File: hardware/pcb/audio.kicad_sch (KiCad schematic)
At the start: 18 parts, among them IC3 TAC5212, J4 PJ-342, J5 PJ-242

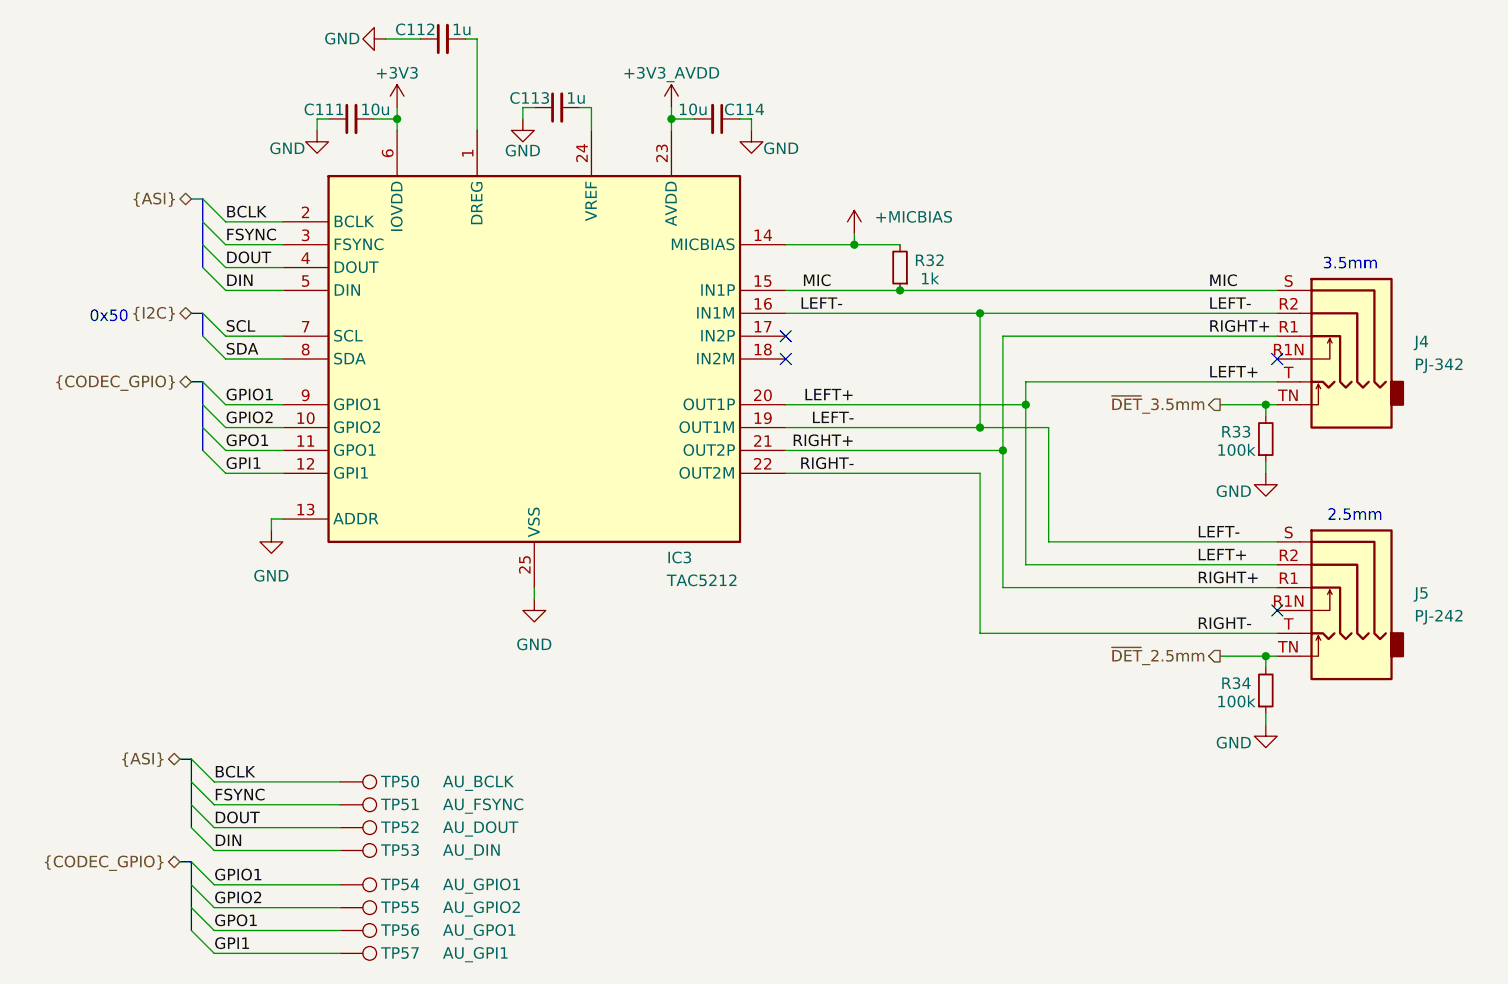
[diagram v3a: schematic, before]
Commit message: added capacitor to sama ddr vref pin
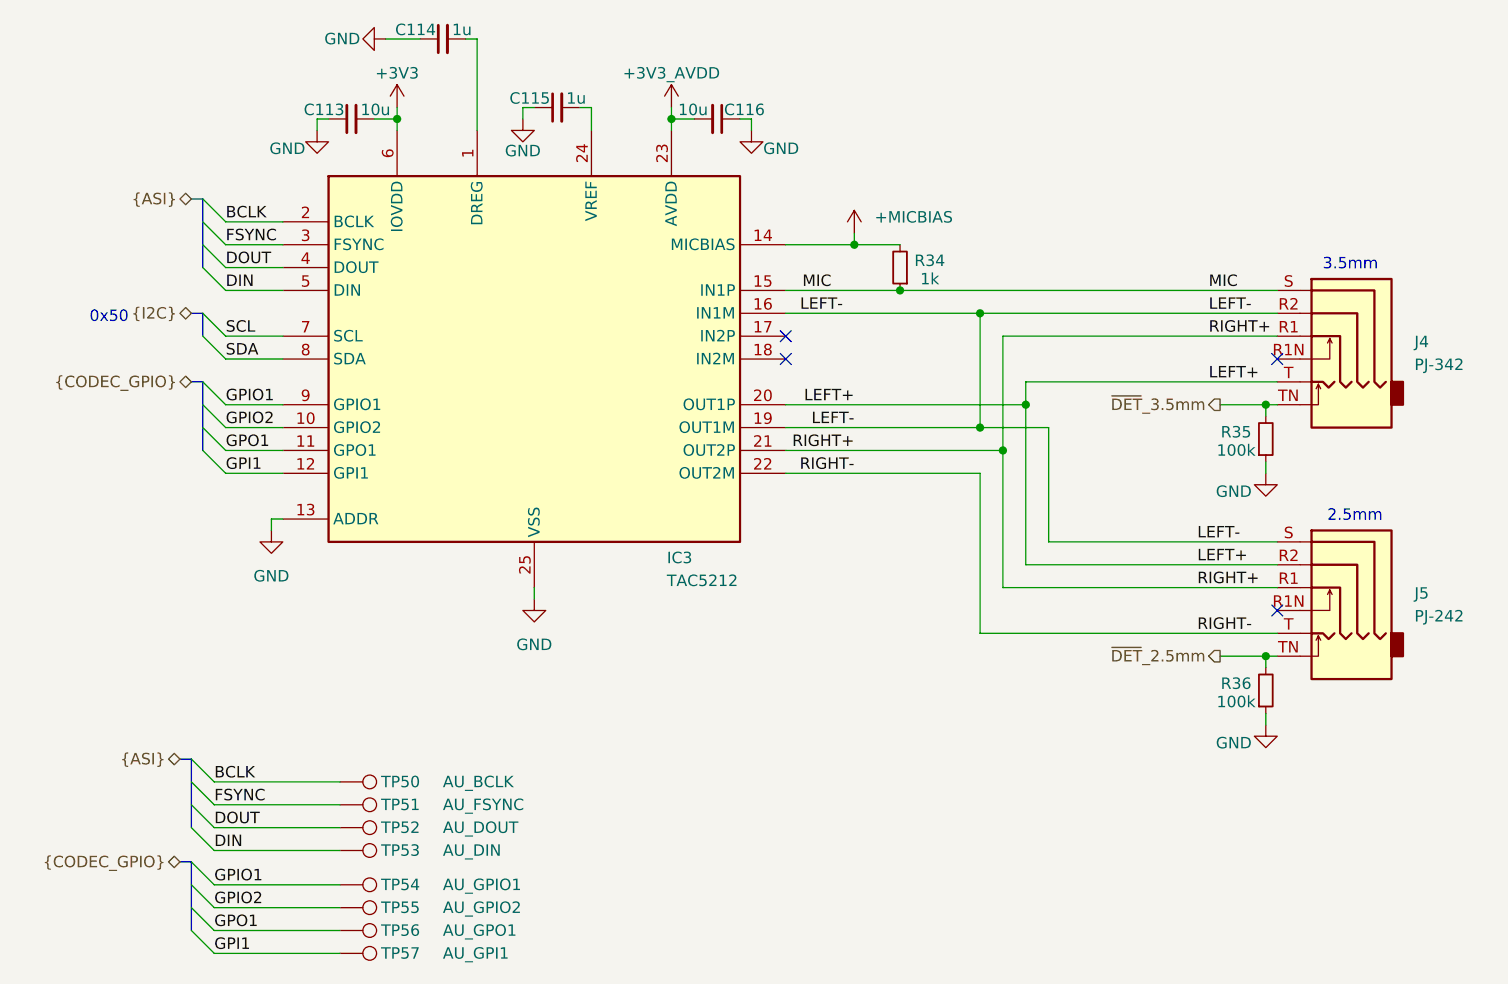
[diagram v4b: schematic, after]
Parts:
- renumbered C111 to C113, C112 to C114, C113 to C115, C114 to C116, R32 to R34, R33 to R35, R34 to R36
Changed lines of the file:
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@@
 		(in_pos_files yes)
 		(dnp no)
-		(property "Reference" "#PWR0106"
+		(property "Reference" "#PWR0108"
 			(at 58.42 33.02 0)
 			(hide yes)
@@
 			(project "meko"
 				(path "/da54f10a-146b-4941-a9c7-55c7173bb101/073f6085-34ed-486a-9dc9-0ac1ede2fab6"
-					(reference "#PWR0106")
+					(reference "#PWR0108")
 					(unit 1)
 				)
@@
 		(in_pos_files yes)
 		(dnp no)
-		(property "Reference" "C111"
+		(property "Reference" "C113"
 			(at 52.578 29.464 90)
 			(show_name no)
@@
 			(project "meko"
 				(path "/da54f10a-146b-4941-a9c7-55c7173bb101/073f6085-34ed-486a-9dc9-0ac1ede2fab6"
-					(reference "C111")
+					(reference "C113")
 					(unit 1)
 				)
@@
 		(in_pos_files yes)
 		(dnp no)
-		(property "Reference" "C112"
+		(property "Reference" "C114"
 			(at 62.738 20.574 90)
 			(show_name no)
@@
 			(project "meko"
 				(path "/da54f10a-146b-4941-a9c7-55c7173bb101/073f6085-34ed-486a-9dc9-0ac1ede2fab6"
-					(reference "C112")
+					(reference "C114")
 					(unit 1)
 				)
@@
 		(dnp no)
 		(fields_autoplaced yes)
-		(property "Reference" "#PWR0103"
+		(property "Reference" "#PWR0105"
 			(at 44.45 82.55 0)
 			(hide yes)
@@
 			(project "meko"
 				(path "/da54f10a-146b-4941-a9c7-55c7173bb101/073f6085-34ed-486a-9dc9-0ac1ede2fab6"
-					(reference "#PWR0103")
+					(reference "#PWR0105")
 					(unit 1)
 				)
@@
 		(in_pos_files yes)
 		(dnp no)
-		(property "Reference" "#PWR0110"
+		(property "Reference" "#PWR0112"
 			(at 97.79 38.1 0)
 			(hide yes)
@@
 			(project "meko"
 				(path "/da54f10a-146b-4941-a9c7-55c7173bb101/073f6085-34ed-486a-9dc9-0ac1ede2fab6"
-					(reference "#PWR0110")
+					(reference "#PWR0112")
 					(unit 1)
 				)
@@
 		(in_pos_files yes)
 		(dnp no)
-		(property "Reference" "R34"
+		(property "Reference" "R36"
 			(at 151.638 93.218 0)
 			(show_name no)
@@
 			(project "meko"
 				(path "/da54f10a-146b-4941-a9c7-55c7173bb101/073f6085-34ed-486a-9dc9-0ac1ede2fab6"
-					(reference "R34")
+					(reference "R36")
 					(unit 1)
 				)
@@
 		(in_pos_files yes)
 		(dnp no)
-		(property "Reference" "#PWR0109"
+		(property "Reference" "#PWR0111"
 			(at 88.9 33.02 0)
 			(hide yes)
@@
 			(project "meko"
 				(path "/da54f10a-146b-4941-a9c7-55c7173bb101/073f6085-34ed-486a-9dc9-0ac1ede2fab6"
-					(reference "#PWR0109")
+					(reference "#PWR0111")
 					(unit 1)
 				)
@@
 		(in_pos_files yes)
 		(dnp no)
-		(property "Reference" "R33"
+		(property "Reference" "R35"
 			(at 151.638 65.278 0)
 			(show_name no)
@@
 			(project "meko"
 				(path "/da54f10a-146b-4941-a9c7-55c7173bb101/073f6085-34ed-486a-9dc9-0ac1ede2fab6"
-					(reference "R33")
+					(reference "R35")
 					(unit 1)
 				)
@@
 		(in_pos_files yes)
 		(dnp no)
-		(property "Reference" "#PWR0104"
+		(property "Reference" "#PWR0106"
 			(at 49.53 38.1 0)
 			(hide yes)
@@
 			(project "meko"
 				(path "/da54f10a-146b-4941-a9c7-55c7173bb101/073f6085-34ed-486a-9dc9-0ac1ede2fab6"
-					(reference "#PWR0104")
+					(reference "#PWR0106")
 					(unit 1)
 				)
@@
 		(in_pos_files yes)
 		(dnp no)
-		(property "Reference" "#PWR0112"
+		(property "Reference" "#PWR0114"
 			(at 154.94 76.2 0)
 			(hide yes)
@@
 			(project "meko"
 				(path "/da54f10a-146b-4941-a9c7-55c7173bb101/073f6085-34ed-486a-9dc9-0ac1ede2fab6"
-					(reference "#PWR0112")
+					(reference "#PWR0114")
 					(unit 1)
 				)
@@
 		(in_pos_files yes)
 		(dnp no)
-		(property "Reference" "#PWR0105"
+		(property "Reference" "#PWR0107"
 			(at 50.8 21.59 0)
 			(hide yes)
@@
 			(project "meko"
 				(path "/da54f10a-146b-4941-a9c7-55c7173bb101/073f6085-34ed-486a-9dc9-0ac1ede2fab6"
-					(reference "#PWR0105")
+					(reference "#PWR0107")
 					(unit 1)
 				)
@@
 		(in_pos_files yes)
 		(dnp no)
-		(property "Reference" "#PWR0107"
+		(property "Reference" "#PWR0109"
 			(at 72.39 36.83 0)
 			(hide yes)
@@
 			(project "meko"
 				(path "/da54f10a-146b-4941-a9c7-55c7173bb101/073f6085-34ed-486a-9dc9-0ac1ede2fab6"
-					(reference "#PWR0107")
+					(reference "#PWR0109")
 					(unit 1)
 				)
@@
 		(in_pos_files yes)
 		(dnp no)
-		(property "Reference" "C113"
+		(property "Reference" "C115"
 			(at 75.438 28.194 90)
 			(show_name no)
@@
 			(project "meko"
 				(path "/da54f10a-146b-4941-a9c7-55c7173bb101/073f6085-34ed-486a-9dc9-0ac1ede2fab6"
-					(reference "C113")
+					(reference "C115")
 					(unit 1)
 				)
@@
 		(in_pos_files yes)
 		(dnp no)
-		(property "Reference" "#PWR0111"
+		(property "Reference" "#PWR0113"
 			(at 109.22 46.99 0)
 			(hide yes)
@@
 			(project "meko"
 				(path "/da54f10a-146b-4941-a9c7-55c7173bb101/073f6085-34ed-486a-9dc9-0ac1ede2fab6"
-					(reference "#PWR0111")
+					(reference "#PWR0113")
 					(unit 1)
 				)
@@
 		(in_pos_files yes)
 		(dnp no)
-		(property "Reference" "C114"
+		(property "Reference" "C116"
 			(at 94.742 29.464 90)
 			(show_name no)
@@
 			(project "meko"
 				(path "/da54f10a-146b-4941-a9c7-55c7173bb101/073f6085-34ed-486a-9dc9-0ac1ede2fab6"
-					(reference "C114")
+					(reference "C116")
 					(unit 1)
 				)
@@
 		(dnp no)
 		(fields_autoplaced yes)
-		(property "Reference" "#PWR0108"
+		(property "Reference" "#PWR0110"
 			(at 73.66 90.17 0)
 			(hide yes)
@@
 			(project "meko"
 				(path "/da54f10a-146b-4941-a9c7-55c7173bb101/073f6085-34ed-486a-9dc9-0ac1ede2fab6"
-					(reference "#PWR0108")
+					(reference "#PWR0110")
 					(unit 1)
 				)
@@
 		(in_pos_files yes)
 		(dnp no)
-		(property "Reference" "R32"
+		(property "Reference" "R34"
 			(at 117.602 46.228 0)
 			(show_name no)
@@
 			(project "meko"
 				(path "/da54f10a-146b-4941-a9c7-55c7173bb101/073f6085-34ed-486a-9dc9-0ac1ede2fab6"
-					(reference "R32")
+					(reference "R34")
 					(unit 1)
 				)
@@
 		(in_pos_files yes)
 		(dnp no)
-		(property "Reference" "#PWR0113"
+		(property "Reference" "#PWR0115"
 			(at 154.94 104.14 0)
 			(hide yes)
@@
 			(project "meko"
 				(path "/da54f10a-146b-4941-a9c7-55c7173bb101/073f6085-34ed-486a-9dc9-0ac1ede2fab6"
-					(reference "#PWR0113")
-					(unit 1)
-				)
+					(reference "#PWR0115")
+					(unit 1)
+				)

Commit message: didn't save last time :sob:
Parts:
- renumbered C113 to C114, C114 to C115, C115 to C116, C116 to C117
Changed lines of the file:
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@@
 		(in_pos_files yes)
 		(dnp no)
-		(property "Reference" "#PWR0108"
+		(property "Reference" "#PWR0109"
 			(at 58.42 33.02 0)
 			(hide yes)
@@
 			(project "meko"
 				(path "/da54f10a-146b-4941-a9c7-55c7173bb101/073f6085-34ed-486a-9dc9-0ac1ede2fab6"
-					(reference "#PWR0108")
+					(reference "#PWR0109")
 					(unit 1)
 				)
@@
 		(in_pos_files yes)
 		(dnp no)
-		(property "Reference" "C113"
+		(property "Reference" "C114"
 			(at 52.578 29.464 90)
 			(show_name no)
@@
 			(project "meko"
 				(path "/da54f10a-146b-4941-a9c7-55c7173bb101/073f6085-34ed-486a-9dc9-0ac1ede2fab6"
-					(reference "C113")
+					(reference "C114")
 					(unit 1)
 				)
@@
 		(in_pos_files yes)
 		(dnp no)
-		(property "Reference" "C114"
+		(property "Reference" "C115"
 			(at 62.738 20.574 90)
 			(show_name no)
@@
 			(project "meko"
 				(path "/da54f10a-146b-4941-a9c7-55c7173bb101/073f6085-34ed-486a-9dc9-0ac1ede2fab6"
-					(reference "C114")
+					(reference "C115")
 					(unit 1)
 				)
@@
 		(dnp no)
 		(fields_autoplaced yes)
-		(property "Reference" "#PWR0105"
+		(property "Reference" "#PWR0106"
 			(at 44.45 82.55 0)
 			(hide yes)
@@
 			(project "meko"
 				(path "/da54f10a-146b-4941-a9c7-55c7173bb101/073f6085-34ed-486a-9dc9-0ac1ede2fab6"
-					(reference "#PWR0105")
+					(reference "#PWR0106")
 					(unit 1)
 				)
@@
 		(in_pos_files yes)
 		(dnp no)
-		(property "Reference" "#PWR0112"
+		(property "Reference" "#PWR0113"
 			(at 97.79 38.1 0)
 			(hide yes)
@@
 			(project "meko"
 				(path "/da54f10a-146b-4941-a9c7-55c7173bb101/073f6085-34ed-486a-9dc9-0ac1ede2fab6"
-					(reference "#PWR0112")
+					(reference "#PWR0113")
 					(unit 1)
 				)
@@
 		(in_pos_files yes)
 		(dnp no)
-		(property "Reference" "#PWR0111"
+		(property "Reference" "#PWR0112"
 			(at 88.9 33.02 0)
 			(hide yes)
@@
 			(project "meko"
 				(path "/da54f10a-146b-4941-a9c7-55c7173bb101/073f6085-34ed-486a-9dc9-0ac1ede2fab6"
-					(reference "#PWR0111")
+					(reference "#PWR0112")
 					(unit 1)
 				)
@@
 		(in_pos_files yes)
 		(dnp no)
-		(property "Reference" "#PWR0106"
+		(property "Reference" "#PWR0107"
 			(at 49.53 38.1 0)
 			(hide yes)
@@
 			(project "meko"
 				(path "/da54f10a-146b-4941-a9c7-55c7173bb101/073f6085-34ed-486a-9dc9-0ac1ede2fab6"
-					(reference "#PWR0106")
+					(reference "#PWR0107")
 					(unit 1)
 				)
@@
 		(in_pos_files yes)
 		(dnp no)
-		(property "Reference" "#PWR0114"
+		(property "Reference" "#PWR0115"
 			(at 154.94 76.2 0)
 			(hide yes)
@@
 			(project "meko"
 				(path "/da54f10a-146b-4941-a9c7-55c7173bb101/073f6085-34ed-486a-9dc9-0ac1ede2fab6"
-					(reference "#PWR0114")
+					(reference "#PWR0115")
 					(unit 1)
 				)
@@
 		(in_pos_files yes)
 		(dnp no)
-		(property "Reference" "#PWR0107"
+		(property "Reference" "#PWR0108"
 			(at 50.8 21.59 0)
 			(hide yes)
@@
 			(project "meko"
 				(path "/da54f10a-146b-4941-a9c7-55c7173bb101/073f6085-34ed-486a-9dc9-0ac1ede2fab6"
-					(reference "#PWR0107")
+					(reference "#PWR0108")
 					(unit 1)
 				)
@@
 		(in_pos_files yes)
 		(dnp no)
-		(property "Reference" "#PWR0109"
+		(property "Reference" "#PWR0110"
 			(at 72.39 36.83 0)
 			(hide yes)
@@
 			(project "meko"
 				(path "/da54f10a-146b-4941-a9c7-55c7173bb101/073f6085-34ed-486a-9dc9-0ac1ede2fab6"
-					(reference "#PWR0109")
+					(reference "#PWR0110")
 					(unit 1)
 				)
@@
 		(in_pos_files yes)
 		(dnp no)
-		(property "Reference" "C115"
+		(property "Reference" "C116"
 			(at 75.438 28.194 90)
 			(show_name no)
@@
 			(project "meko"
 				(path "/da54f10a-146b-4941-a9c7-55c7173bb101/073f6085-34ed-486a-9dc9-0ac1ede2fab6"
-					(reference "C115")
+					(reference "C116")
 					(unit 1)
 				)
@@
 		(in_pos_files yes)
 		(dnp no)
-		(property "Reference" "#PWR0113"
+		(property "Reference" "#PWR0114"
 			(at 109.22 46.99 0)
 			(hide yes)
@@
 			(project "meko"
 				(path "/da54f10a-146b-4941-a9c7-55c7173bb101/073f6085-34ed-486a-9dc9-0ac1ede2fab6"
-					(reference "#PWR0113")
+					(reference "#PWR0114")
 					(unit 1)
 				)
@@
 		(in_pos_files yes)
 		(dnp no)
-		(property "Reference" "C116"
+		(property "Reference" "C117"
 			(at 94.742 29.464 90)
 			(show_name no)
@@
 			(project "meko"
 				(path "/da54f10a-146b-4941-a9c7-55c7173bb101/073f6085-34ed-486a-9dc9-0ac1ede2fab6"
-					(reference "C116")
+					(reference "C117")
 					(unit 1)
 				)
@@
 		(dnp no)
 		(fields_autoplaced yes)
-		(property "Reference" "#PWR0110"
+		(property "Reference" "#PWR0111"
 			(at 73.66 90.17 0)
 			(hide yes)
@@
 			(project "meko"
 				(path "/da54f10a-146b-4941-a9c7-55c7173bb101/073f6085-34ed-486a-9dc9-0ac1ede2fab6"
-					(reference "#PWR0110")
+					(reference "#PWR0111")
 					(unit 1)
 				)
@@
 		(in_pos_files yes)
 		(dnp no)
-		(property "Reference" "#PWR0115"
+		(property "Reference" "#PWR0116"
 			(at 154.94 104.14 0)
 			(hide yes)
@@
 			(project "meko"
 				(path "/da54f10a-146b-4941-a9c7-55c7173bb101/073f6085-34ed-486a-9dc9-0ac1ede2fab6"
-					(reference "#PWR0115")
-					(unit 1)
-				)
+					(reference "#PWR0116")
+					(unit 1)
+				)
